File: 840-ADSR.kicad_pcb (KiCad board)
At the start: 2 copper layers, 38 x 106 mm, 97 parts, among them J1 PJ-301B-JACK, J2 PJ-301B-JACK, J3 PJ-301B-JACK, J4 PJ-301B-JACK, J5 PJ-301B, J6 PJ-301B, J7 PJ-301B, P1 CONN_02X05, Q1 MMBT3904, Q2 MMBT3904, Q3 MMBT3904, Q4 DMMT3904W, Q5 DMMT3906W-K4B, SW1 B3F-1050, T1 10K, T2 10K, U1 CD4052, U2 NE555, U3 TL074-, U4 TL072-

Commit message: parts mostly placed, starting to route
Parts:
- removed C10, C11, C12, C13, C14, C15, C16, C8, C9: 0.1µ, MyModules:SM0603-C-MURATA
- C1, C19, C2, C20, C21, C22, C23, C24, C3, C4, C5, C6, C7, D4, D5, Q1, Q2, Q3, Q4, Q5, R1, R10, R11, R12, R13, R14, R15, R16, R17, R18, R19, R2, R20, R21, R22, R23, R24, R25, R26, R27, R28, R29, R3, R30, R31, R32, R33, R34, R35, R36, R37, R38, R39, R4, R40, R5, R7, R8, R9, T1, T2, U1, U2, U3, U4: moved to B.Cu
- moved R1 108.9 mm to (84.0, 57.2), turned to 270 degrees
- moved C1 92.6 mm to (106.5, 72.8), turned to 180 degrees
- moved R2 85.1 mm to (84.2, 81.2), turned to 90 degrees
- moved R35 75.0 mm to (87.5, 91.0), turned to 180 degrees
- moved D4 72.6 mm to (85.2, 93.8), turned to 270 degrees
- moved C24 72.1 mm to (88.5, 93.8), turned to 270 degrees
- moved C2 64.2 mm to (109.8, 101.8)
- moved R3 61.9 mm to (84.2, 105.0), turned to 90 degrees
- moved C3 57.9 mm to (92.5, 107.5)
- moved R21 57.0 mm to (111.5, 109.5), turned to 180 degrees
- moved R10 56.2 mm to (88.0, 110.0), turned to 270 degrees
- moved R17 55.4 mm to (115.0, 112.0), turned to 270 degrees
- moved R18 54.6 mm to (100.5, 110.5)
- moved U1 53.8 mm to (94.5, 111.5), turned to 180 degrees
- moved R22 52.2 mm to (116.8, 116.0), turned to 270 degrees
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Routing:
- net +10V: track 0.00 -> 88.8 mm
- net +12V: track 0.00 -> 67.9 mm
- net -12V: track 0.00 -> 32.6 mm, vias 0 -> 3
- net Net-(C22-Pad2): track 0.00 -> 27.2 mm, vias 0 -> 2
- net Net-(C22-Pad1): track 0.00 -> 23.1 mm
- net Net-(C23-Pad2): track 0.00 -> 23.0 mm, vias 0 -> 3
- net Net-(R26-Pad2): track 0.00 -> 10.9 mm
- net Net-(Q5-Pad1): track 0.00 -> 10.1 mm
- net Net-(R27-Pad2): track 0.00 -> 8.23 mm
- net Net-(C23-Pad1): track 0.00 -> 7.29 mm
- net Net-(R39-Pad2): track 0.00 -> 6.71 mm
- net Net-(Q4-Pad4): track 0.00 -> 6.39 mm
- net Net-(R25-Pad2): track 0.00 -> 6.03 mm
- net Net-(R23-Pad2): track 0.00 -> 5.26 mm
- net Net-(Q4-Pad1): track 0.00 -> 5.02 mm
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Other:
- net class Default: via_dia 0.6 -> 0.9; via_drill 0.4 -> 0.45
- net class POWER added: clearance 0.3, trace_width 0.35, via_dia 1.2, via_drill 0.6

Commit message: almost done routing
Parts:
- removed R1, R2, R3, R4: 10K, MyModules:SM0603-R-YAGEO
- P1: moved to B.Cu
- moved C2 38.3 mm to (115.5, 139.6), turned to 90 degrees
- moved C3 36.3 mm to (113.8, 136.8)
- moved C4 31.4 mm to (104.8, 98.2), turned to 270 degrees
- moved P1 30.9 mm to (95.2, 75.0), turned to 0 degrees
- moved D2 30.8 mm to (106.2, 73.8), turned to 270 degrees
- moved F2 29.0 mm to (96.5, 78.2), turned to 0 degrees
- moved C17 28.6 mm to (86.5, 65.2), turned to 0 degrees
- moved F1 28.4 mm to (96.2, 61.8)
- moved R23 25.9 mm to (110.8, 109.0), turned to 0 degrees
- moved R27 25.5 mm to (110.8, 101.5), turned to 180 degrees
- moved C22 24.1 mm to (111.5, 118.8), turned to 180 degrees
- moved R28 24.0 mm to (106.5, 98.2), turned to 270 degrees
- moved R31 23.9 mm to (108.2, 98.2), turned to 90 degrees
- moved D1 22.2 mm to (95.2, 56.0), turned to 90 degrees
- moved C18 21.8 mm to (112.8, 76.0), turned to 0 degrees
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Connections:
- J1 pad 2: Net-(J1-Pad2) -> +10V
- J2 pad 2: Net-(J2-Pad2) -> +10V
- J3 pad 2: Net-(J3-Pad2) -> +10V
- J4 pad 2: Net-(J4-Pad2) -> +10V
- Q5 pad 1: Net-(Q5-Pad1) -> GND
- Q5 pad 2: GND -> Net-(Q5-Pad2)
- Q5 pad 3: Net-(C22-Pad2) -> Net-(C23-Pad2)
- Q5 pad 6: Net-(C23-Pad2) -> Net-(C22-Pad2)
- R19 pad 2: Net-(Q5-Pad1) -> Net-(Q5-Pad2)
- R20 pad 2: Net-(Q5-Pad1) -> Net-(Q5-Pad2)
- T1 pad 2: Net-(Q5-Pad1) -> Net-(Q5-Pad2)
- T1 pad 3: Net-(Q5-Pad1) -> Net-(Q5-Pad2)
- U3 pad 1: Net-(R32-Pad2) -> Net-(C22-Pad1)
- U3 pad 10: GND -> Net-(R26-Pad2)
- U3 pad 2: Net-(R25-Pad2) -> Net-(C22-Pad2)
- U3 pad 3: Net-(R26-Pad2) -> GND
- U3 pad 8: Net-(C22-Pad1) -> Net-(R32-Pad2)
- U3 pad 9: Net-(C22-Pad2) -> Net-(R25-Pad2)
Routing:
- net +12V: track 67.9 -> 309.4 mm, vias 0 -> 7
- net Net-(R5-Pad1): track 0.00 -> 102.1 mm, vias 0 -> 1
- net -12V: track 32.6 -> 127.4 mm, vias 3 -> 4
- net GND: track 0.00 -> 79.1 mm, vias 0 -> 16
- net ATTACK: track 1.65 -> 74.6 mm, vias 1 -> 0
- net DECAY: track 0.00 -> 69.8 mm
- net Net-(R32-Pad2): track 2.92 -> 62.2 mm, vias 0 -> 2
- net Net-(C23-Pad1): track 7.29 -> 58.9 mm, vias 0 -> 2
- net Net-(R28-Pad1): track 0.00 -> 35.0 mm, vias 0 -> 2
- net Net-(D5-Pad1): track 0.00 -> 26.8 mm
- net Net-(J3-Pad3): track 0.00 -> 24.5 mm
- net Net-(J2-Pad3): track 0.00 -> 22.7 mm
- net Net-(J1-Pad3): track 0.00 -> 22.7 mm
- net Net-(J4-Pad3): track 0.00 -> 21.7 mm
- net Net-(Q3-Pad1): track 0.00 -> 19.5 mm
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- added copper zone on B.Cu, net GND
- added copper zone on F.Cu, net GND
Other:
- net class Default: via_dia 0.9 -> 0.8; via_drill 0.45 -> 0.4
- net class POWER: clearance 0.3 -> 0.25; via_dia 1.2 -> 1; via_drill 0.6 -> 0.5

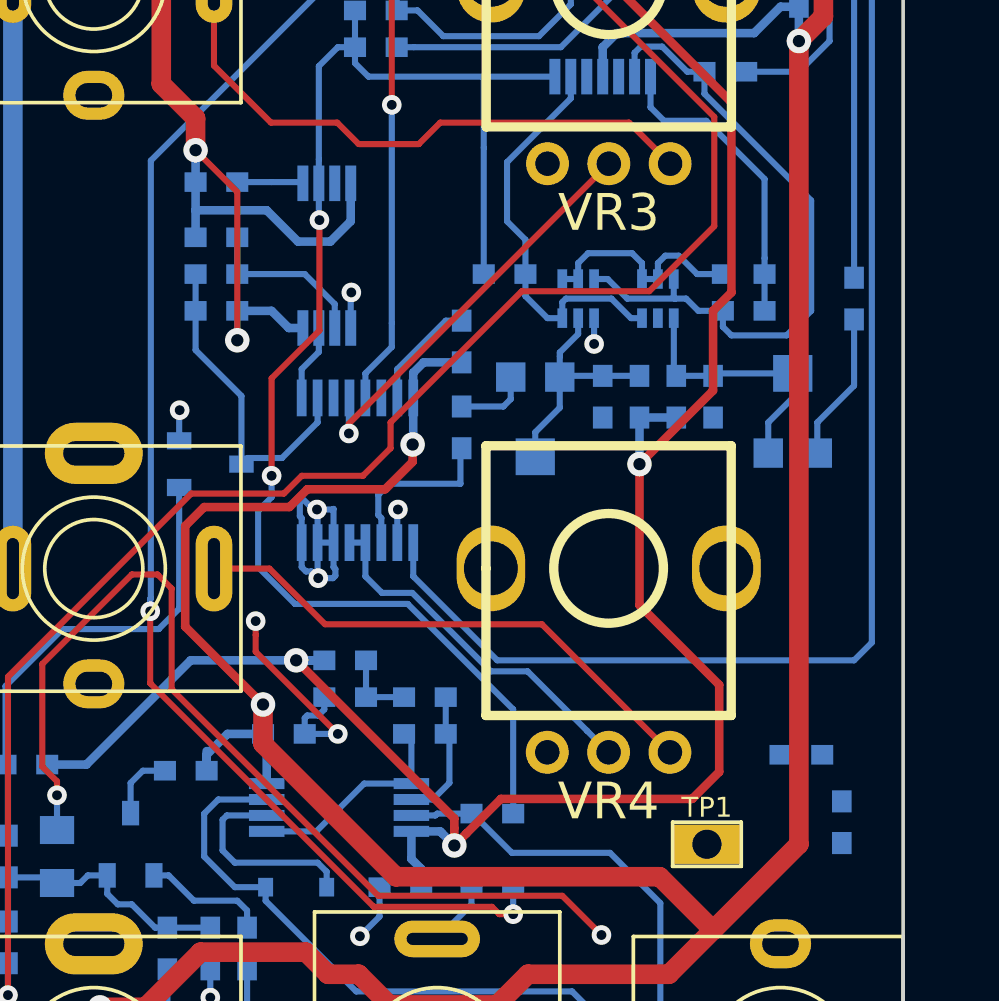
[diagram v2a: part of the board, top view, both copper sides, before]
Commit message: routed, need to place silk screen labels
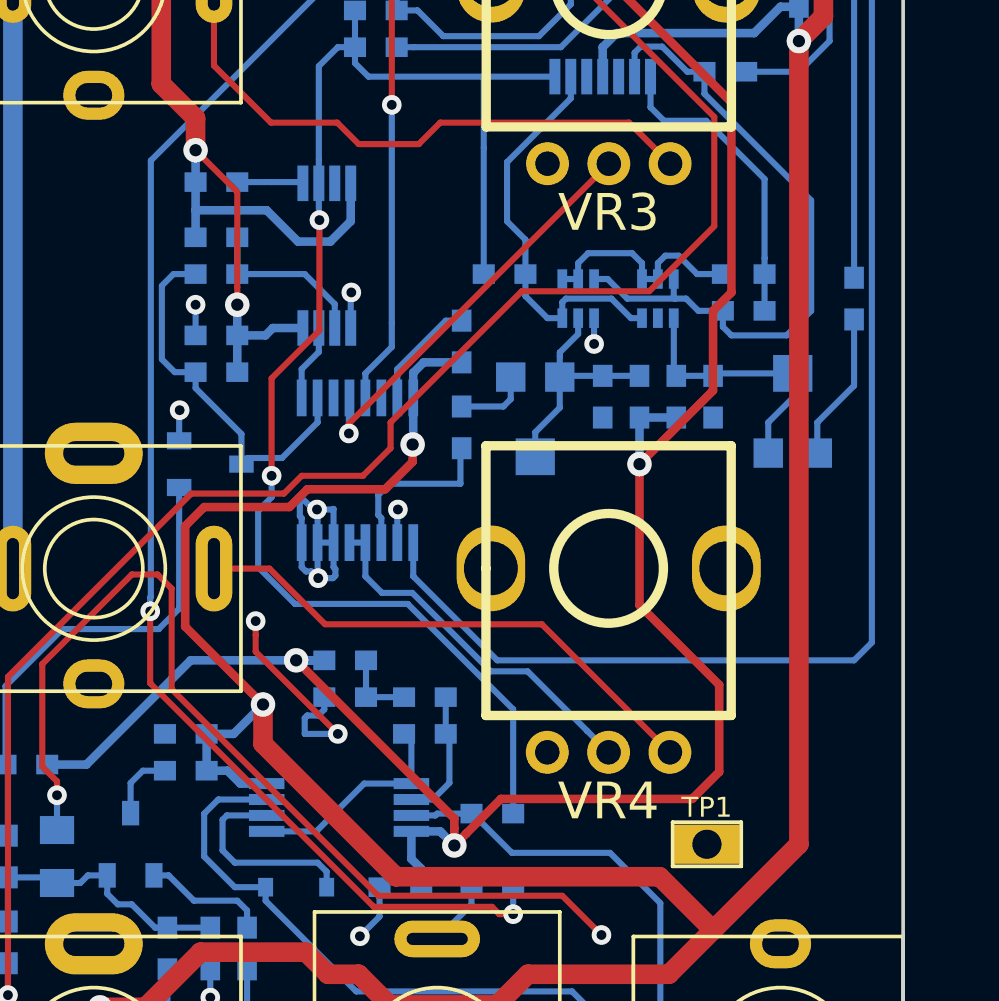
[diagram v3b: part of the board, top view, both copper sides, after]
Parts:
- removed C2: 0.1µ, MyModules:SM0603-C-MURATA
- moved C3 25.1 mm to (88.8, 136.0), turned to 180 degrees
- moved C21 16.5 mm to (90.0, 119.8), turned to 180 degrees
- moved R14 2.50 mm to (90.0, 121.2)
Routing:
- net Net-(C20-Pad1): track 13.3 -> 15.5 mm
- net GND: track 79.1 -> 80.3 mm, vias 16 -> 17

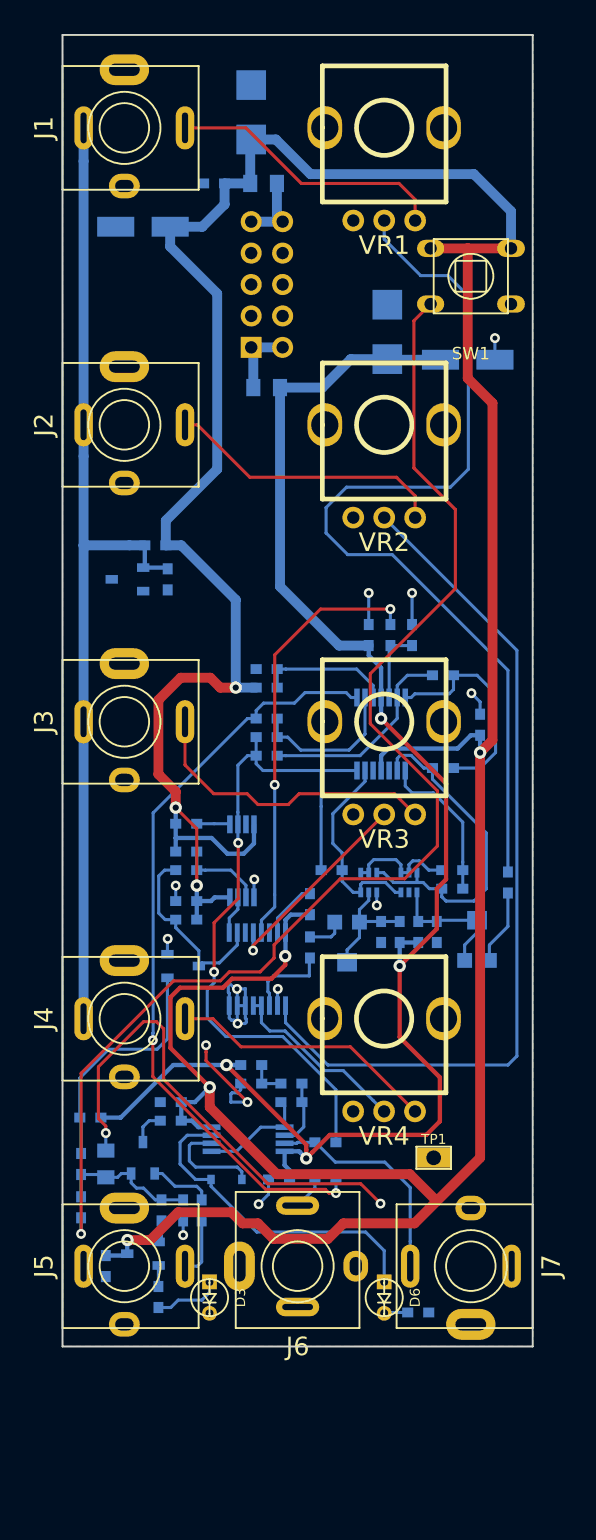
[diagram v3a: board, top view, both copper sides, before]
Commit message: added .gitignore and some silk screen tweaking
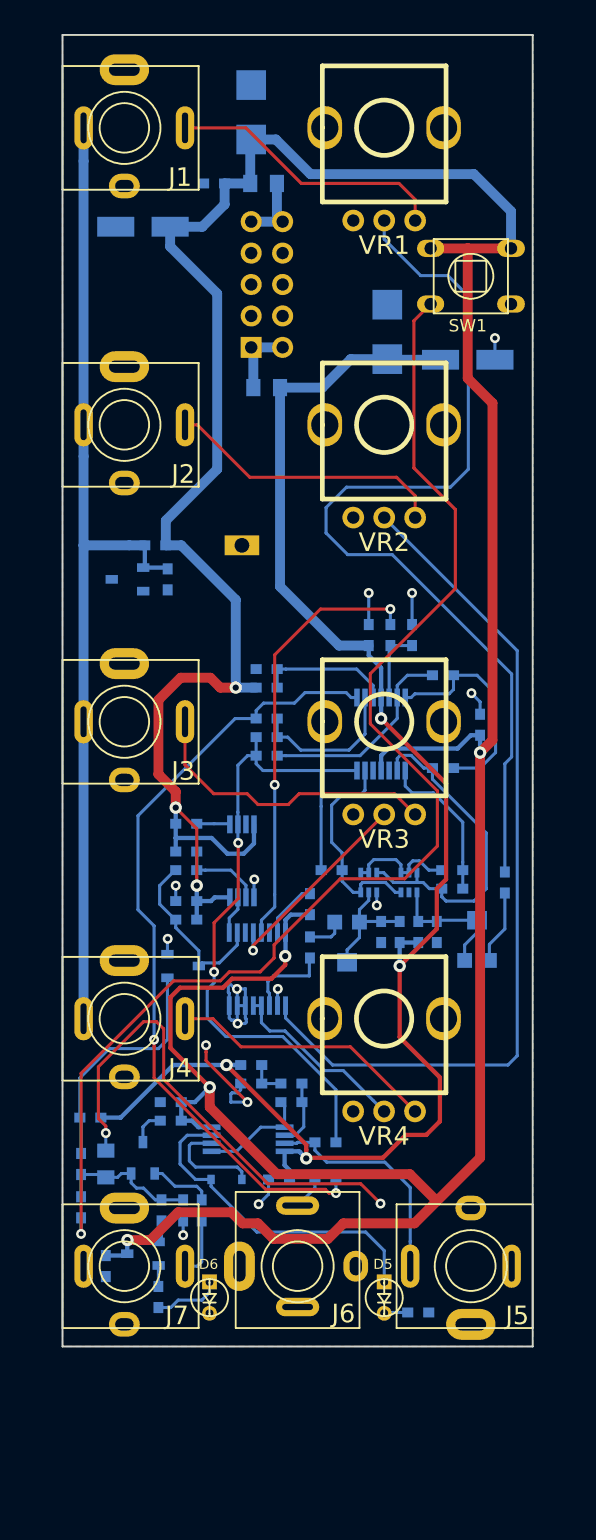
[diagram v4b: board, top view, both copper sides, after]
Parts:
- TP1: moved to B.Cu
- moved TP1 51.9 mm to (94.5, 91.0)
- moved R14 0.25 mm to (115.8, 118.2)
- renumbered C21 to C10, C3 to C11, C19 to C12, C6 to C13, C7 to C14, C17 to C2, C18 to C3, C24 to C4, C4 to C5, C5 to C6, C20 to C7, C23 to C8, C22 to C9, D4 to D3, D5 to D4, D6 to D5, D3 to D6, J7 to J5, J5 to J7, Q5 to Q1, Q4 to Q2, Q1 to Q4, Q2 to Q5, R35 to R1, R23 to R10, R15 to R11, R16 to R12, R24 to R13, R17 to R14, R10 to R15, R14 to R16, R19 to R17, R20 to R18, R22 to R19, R28 to R2, R21 to R20, R18 to R21, R37 to R22, R36 to R23, R38 to R24, R39 to R25, R13 to R26, R7 to R27, R34 to R28, R12 to R29, R31 to R3, R33 to R30, R5 to R31, R8 to R32, R11 to R33, R6 to R34, R9 to R35, R40 to R36, R29 to R4, R27 to R5, R26 to R6, R32 to R7, R25 to R8, R30 to R9, U3 to U1, U1 to U3
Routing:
- net Net-(R30-Pad1): track 62.2 -> 63.8 mm
- net Net-(C7-Pad1): track 15.5 -> 14.5 mm
- net Net-(C8-Pad2): track 16.5 -> 17.5 mm
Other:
- board text added: "ATTACK"
- board text added: "DEC/REL"

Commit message: bit of rail tweaking
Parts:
- moved R28 1.00 mm to (101.2, 138.2), turned to 270 degrees
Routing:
- net -12V: track 127.4 -> 139.3 mm, vias 4 -> 6
- net +12V: track 308.9 -> 318.0 mm, vias 7 -> 9
- net Net-(C8-Pad1): track 58.9 -> 56.7 mm
- net SUSTAIN: track 16.9 -> 18.3 mm
- net Net-(R31-Pad1): track 102.1 -> 103.4 mm
- net Net-(J3-Pad3): track 24.5 -> 25.5 mm
- net GND: track 80.3 -> 80.9 mm, vias 17 -> 18

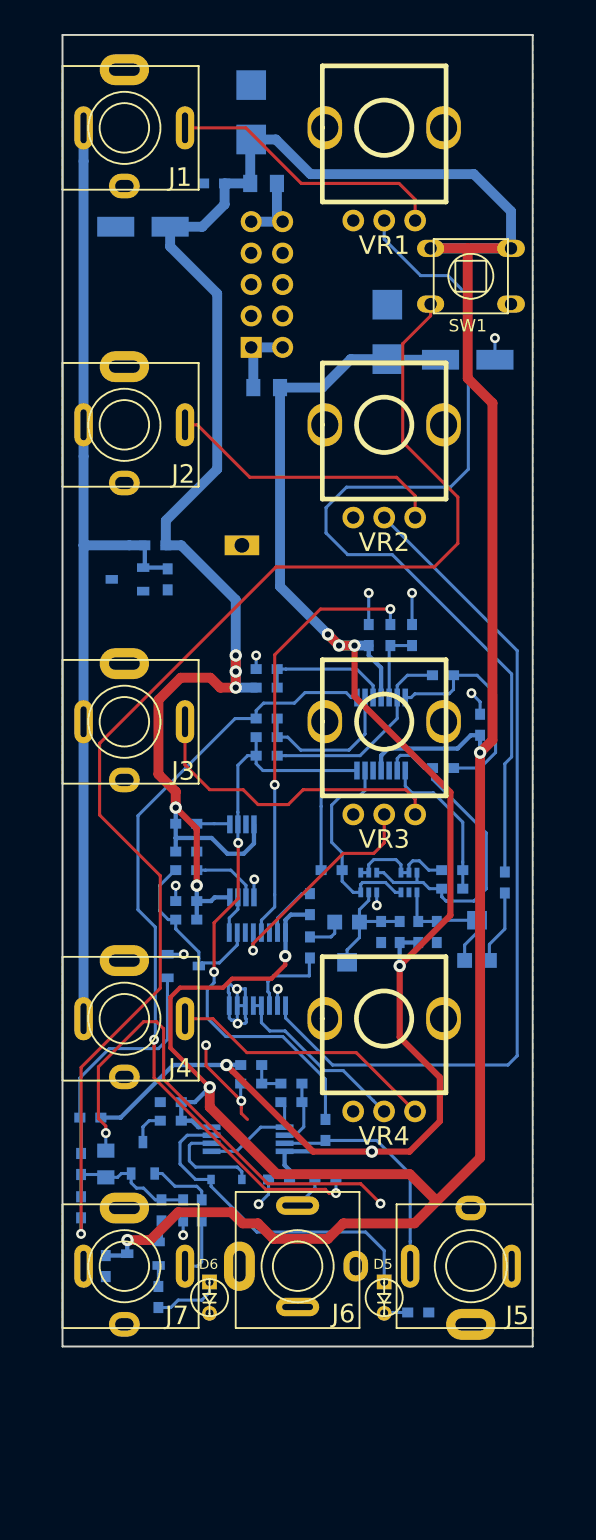
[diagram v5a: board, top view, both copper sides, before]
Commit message: delted 3.3K resistor connected to 555 CV pin and replaced wtih 10V reference. duh.
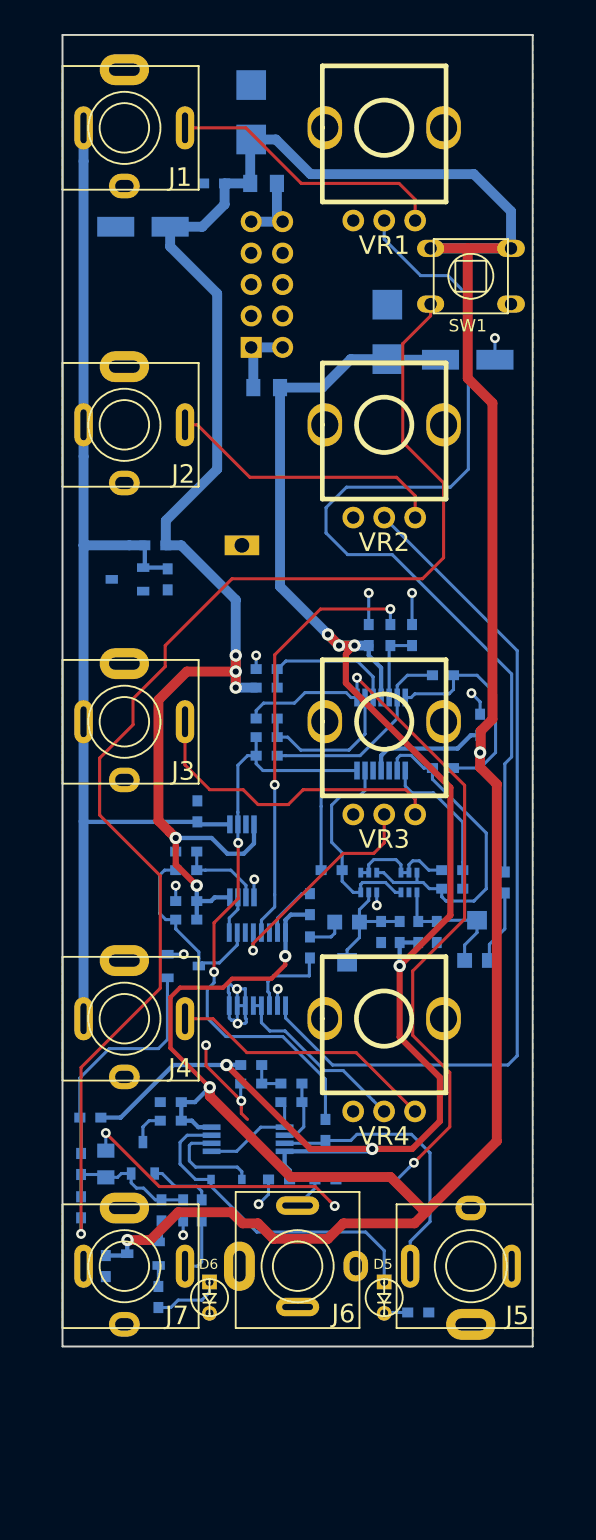
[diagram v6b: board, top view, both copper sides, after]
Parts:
- removed R11: 3.3K**, MyModules:SM0603-R-YAGEO
- added C15: 10n, MyModules:SM0603-C-MURATA, B.Cu at (90.9, 112.5)
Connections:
- U2 pad 5: Net-(R11-Pad1) -> +10V
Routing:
- net GND: track 80.9 -> 63.4 mm
- net +10V: track 80.8 -> 92.8 mm
- net ENV_OUT: track 18.8 -> 22.5 mm
- net Net-(R11-Pad1): track 2.70 -> 0.00 mm
- net +12V: track 318.0 -> 315.5 mm
- net Net-(R30-Pad1): track 63.8 -> 65.0 mm
- net Net-(R4-Pad2): track 10.8 -> 11.7 mm
- net Net-(C7-Pad1): track 14.8 -> 15.4 mm
- net Net-(R31-Pad1): track 103.4 -> 104.0 mm

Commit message: prototype built, needs tweaking, about to start
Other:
- rule pad_to_mask_clearance: 0.2 -> 0.025
- board text added: "+OUT"
- board text added: "840 ADSR"
- board text added: "DECAY"
- board text added: "GATE"
- board text added: "RELEASE"
- board text added: "SUSTAIN"
- board text added: "r1.0 9/2018"
- board text added: "system80.net"
- board text added: "−12V"
- board text added: "−OUT"
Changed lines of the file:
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@@
     (links 188)
     (no_connects 1)
-    (area 79.924999 49.674999 118.075001 155.825001)
+    (area 79.674999 48.149286 118.360714 155.825001)
     (thickness 1.6)
-    (drawings 94)
+    (drawings 106)
     (tracks 615)
     (zones 0)
@@
   )
   (setup
-    (last_trace_width 0.8)
+    (last_trace_width 0.25)
     (user_trace_width 0.25)
     (user_trace_width 0.35)
@@
     (pad_size 1.524 1.524)
     (pad_drill 0.762)
-    (pad_to_mask_clearance 0.2)
+    (pad_to_mask_clearance 0.025)
+    (pad_to_paste_clearance_ratio -0.05)
     (aux_axis_origin 0 0)
-    (visible_elements 7FFFB77F)
+    (visible_elements 7FFFF77F)
     (pcbplotparams
-      (layerselection 0x00030_80000001)
-      (usegerberextensions false)
+      (layerselection 0x010f0_80000001)
+      (usegerberextensions true)
       (excludeedgelayer true)
       (linewidth 0.200000)
@@
       (psnegative false)
       (psa4output false)
-      (plotreference true)
+      (plotreference false)
       (plotvalue true)
       (plotinvisibletext false)
       (padsonsilk false)
-      (subtractmaskfromsilk false)
+      (subtractmaskfromsilk true)
       (outputformat 1)
       (mirror false)
-      (drillshape 1)
+      (drillshape 0)
       (scaleselection 1)
-      (outputdirectory ""))
+      (outputdirectory Gerbers/))
   )
   (net 0 "")
@@
     (descr "Through hole straight pin header, 2x05, 2.54mm pitch, double rows")
     (tags "Through hole pin header THT 2x05 2.54mm double row")
-    (fp_text reference P1 (at 1.27 2.33) (layer B.SilkS)
+    (fp_text reference P1 (at 3.75 -12.75) (layer B.SilkS)
       (effects (font (size 1 1) (thickness 0.15)) (justify mirror))
     )
@@
     )
   )
+  (gr_text ATTACK (at 89.5 51) (layer F.SilkS)
+    (effects (font (size 1 1) (thickness 0.15)))
+  )
+  (gr_text DECAY (at 89.5 75) (layer F.SilkS)
+    (effects (font (size 1 1) (thickness 0.15)))
+  )
+  (gr_text SUSTAIN (at 90.25 99) (layer F.SilkS)
+    (effects (font (size 1 1) (thickness 0.15)))
+  )
+  (gr_text RELEASE (at 89.75 122.75) (layer F.SilkS)
+    (effects (font (size 1 1) (thickness 0.15)))
+  )
+  (gr_text +OUT (at 112.5 142) (layer F.SilkS)
+    (effects (font (size 1 1) (thickness 0.15)))
+  )
+  (gr_text −OUT (at 99 142) (layer F.SilkS)
+    (effects (font (size 1 1) (thickness 0.15)))
+  )
+  (gr_text GATE (at 85 142) (layer F.SilkS)
+    (effects (font (size 1 1) (thickness 0.15)))
+  )
+  (gr_text system80.net (at 99 154.5) (layer B.SilkS)
+    (effects (font (size 0.8 0.8) (thickness 0.15)) (justify mirror))
+  )
+  (gr_text "r1.0 9/2018" (at 99.25 146.75) (layer B.SilkS)
+    (effects (font (size 0.8 0.8) (thickness 0.15)) (justify mirror))
+  )
+  (gr_text "840 ADSR" (at 106.5 52.5) (layer B.SilkS)
+    (effects (font (size 2.5 2.5) (thickness 0.5)) (justify mirror))
+  )
+  (gr_line (start 90.5 75) (end 102.5 75) (layer B.SilkS) (width 1))
+  (gr_text −12V (at 101.5 76.25) (layer B.SilkS)
+    (effects (font (size 0.8 0.8) (thickness 0.15)) (justify mirror))
+  )
   (gr_text DEC/REL (at 103.5 126.5) (layer B.SilkS)
